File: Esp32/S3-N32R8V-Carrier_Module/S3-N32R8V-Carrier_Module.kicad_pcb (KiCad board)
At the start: 2 copper layers, 39.5 x 23 mm, 4 parts, among them J2 DF40HC3.5-30DS-0.4V51, J3 Conn_02x06_Odd_Even

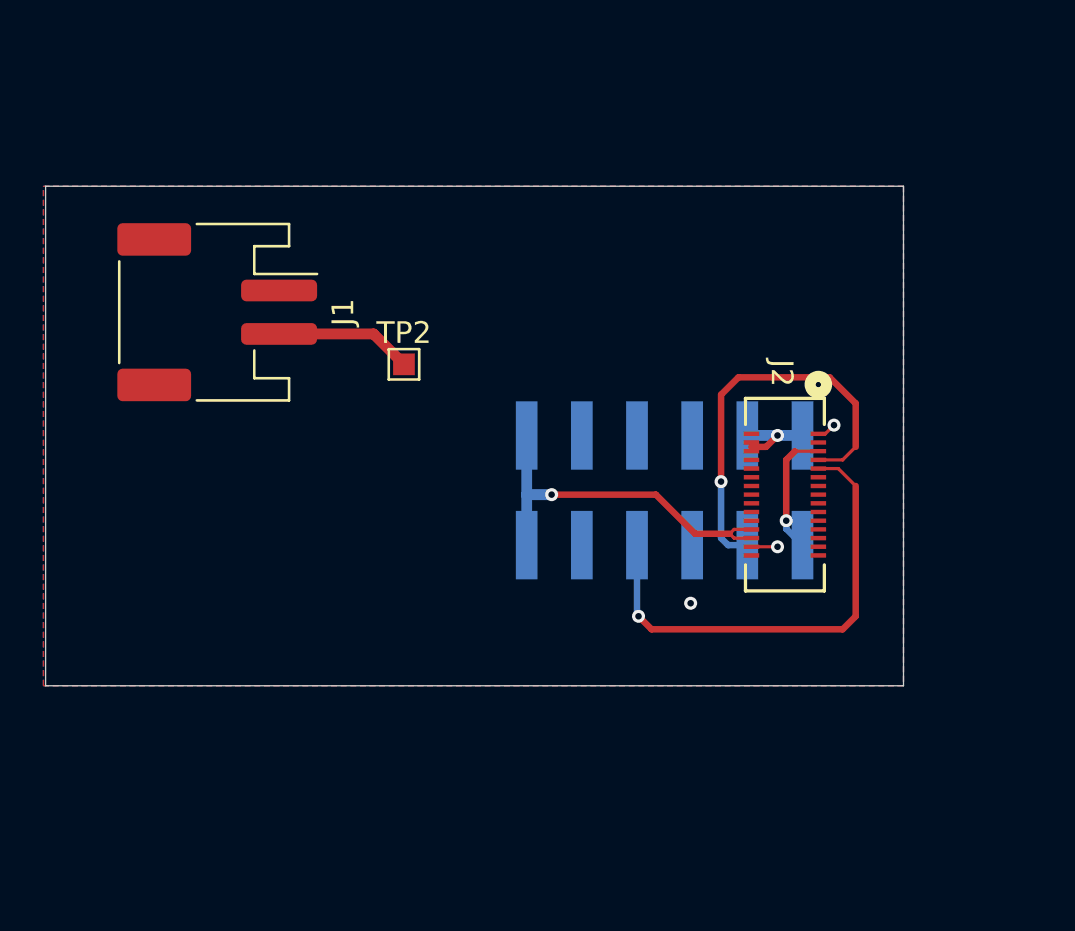
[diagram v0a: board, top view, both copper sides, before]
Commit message: Connector
Modify jst connector (Need to look for the correct One)
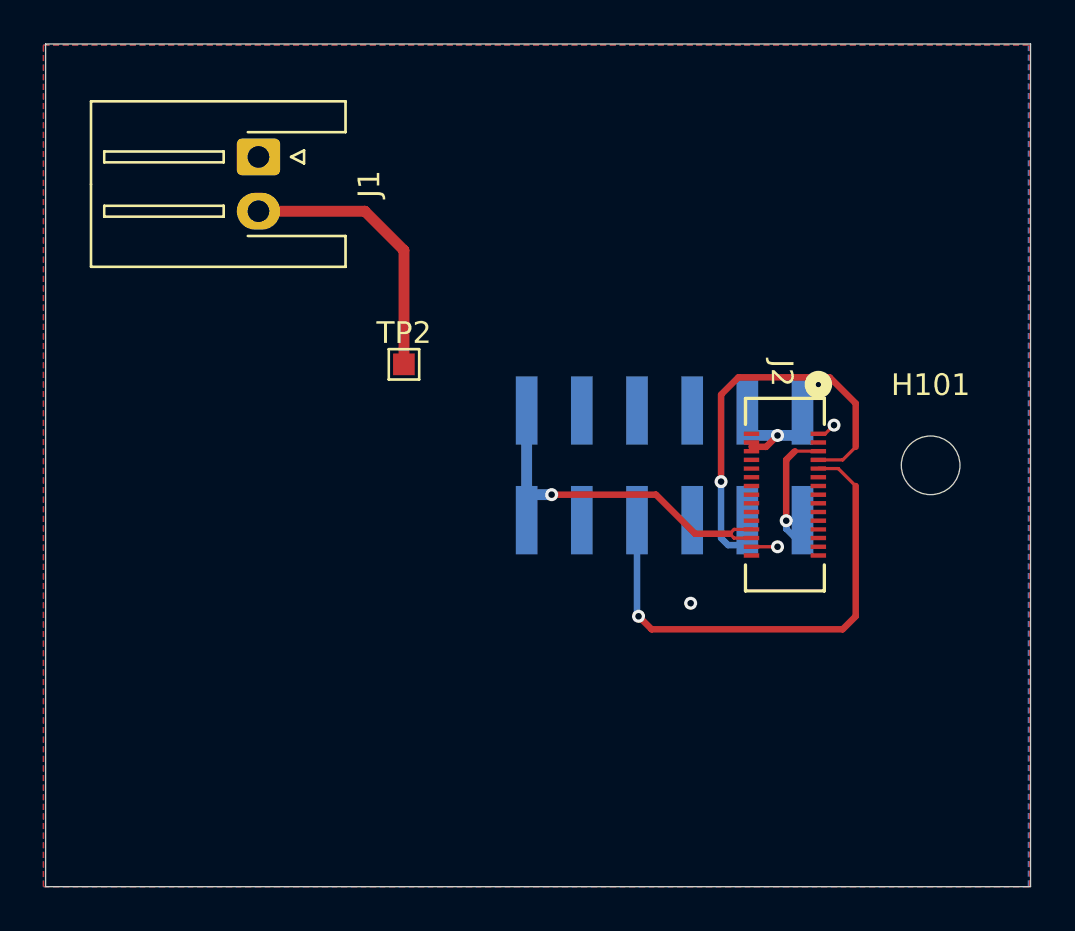
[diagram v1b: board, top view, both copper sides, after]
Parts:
- added H101: MountingHole, MountingHole:MountingHole_2.7mm, F.Cu at (159.2, 94.8)
- J1: footprint Connector_JST:JST_PH_S2B-PH-SM4-TB_1x02-1MP_P2.00mm_Horizontal -> Connector_JST:JST_XH_S2B-XH-A-1_1x02_P2.50mm_Horizontal
- moved J1 7.40 mm to (128.3, 80.7)
- moved J3 1.15 mm to (147.0, 94.8)
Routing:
- net Net-(J1-+): track 6.33 -> 12.7 mm
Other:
- board size 39.5 x 23 mm -> 45.3 x 38.8 mm
